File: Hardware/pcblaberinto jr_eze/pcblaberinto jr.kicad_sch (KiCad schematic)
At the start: 19 parts, among them J1 Ultrasonido, J2 Ultrasonido, J3 Ultrasonido, J4 CableAlimentacion, J5 Jumper, J7 EncoderMotorDerecha, J8 EncoderMotorIzquierda, J9 Input of Driver L9110, SW1 SW_Push, U1 L7805

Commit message: modificaciones a la placa
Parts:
- J1, J2, J3: footprint (none) -> EESTN5:pin_strip_4
- UM1: footprint (none) -> EESTN5:ESP32_DEVKITC
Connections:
- net ECCHO_1: now also UM1.9 (IO27); no longer UM1.8 (IO14)
- net IN3: now also J9.5 (Pin_5); no longer J9.6 (Pin_6)
- net IN4: now also J9.6 (Pin_6); no longer J9.5 (Pin_5)
- net TRIGG_1: now also UM1.10 (IO26); no longer UM1.9 (IO27)
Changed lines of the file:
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@@
+    (stroke (width 0) (type default) (color 0 0 0 0))
+  )
+  (wire (pts (xy 120.65 55.88) (xy 124.46 55.88))
     (stroke (width 0) (type default) (color 0 0 0 0))
   )
@@
     (stroke (width 0) (type default) (color 0 0 0 0))
   )
+  (wire (pts (xy 84.9122 111.379) (xy 87.4522 111.379))
+    (stroke (width 0) (type default) (color 0 0 0 0))
+  )
+  (wire (pts (xy 179.705 43.815) (xy 179.705 47.9298))
+    (stroke (width 0) (type default) (color 0 0 0 0))
+  )
+  (wire (pts (xy 256.4638 49.7332) (xy 259.1816 49.7332))
+    (stroke (width 0) (type default) (color 0 0 0 0))
+  )
+  (wire (pts (xy 29.718 50.038) (xy 33.528 50.038))
+    (stroke (width 0) (type default) (color 0 0 0 0))
+  )
+  (wire (pts (xy 188.595 33.655) (xy 191.77 33.655))
+    (stroke (width 0) (type default) (color 0 0 0 0))
+  )
+  (wire (pts (xy 75.057 68.58) (xy 75.057 69.723))
+    (stroke (width 0) (type default) (color 0 0 0 0))
+  )
+  (wire (pts (xy 216.154 29.3624) (xy 216.154 33.655))
+    (stroke (width 0) (type default) (color 0 0 0 0))
+  )
+  (wire (pts (xy 188.595 43.815) (xy 188.595 47.9298))
+    (stroke (width 0) (type default) (color 0 0 0 0))
+  )
+  (wire (pts (xy 248.539 84.455) (xy 254.5588 84.455))
+    (stroke (width 0) (type default) (color 0 0 0 0))
+  )
+  (polyline (pts (xy 62.23 13.335) (xy 62.23 132.08))
+    (stroke (width 0) (type default) (color 0 0 0 0))
+  )
+  (wire (pts (xy 188.595 47.9298) (xy 188.595 47.9552))
+    (stroke (width 0) (type default) (color 0 0 0 0))
+  )
+  (wire (pts (xy 248.539 97.155) (xy 254.5588 97.155))
+    (stroke (width 0) (type default) (color 0 0 0 0))
+  )
+  (wire (pts (xy 29.718 47.498) (xy 33.528 47.498))
+    (stroke (width 0) (type default) (color 0 0 0 0))
+  )
+  (wire (pts (xy 29.972 62.484) (xy 33.782 62.484))
+    (stroke (width 0) (type default) (color 0 0 0 0))
+  )
+  (wire (pts (xy 179.705 38.735) (xy 179.705 33.655))
+    (stroke (width 0) (type default) (color 0 0 0 0))
+  )
+  (polyline (pts (xy 232.41 12.7) (xy 232.41 111.76))
+    (stroke (width 0) (type default) (color 0 0 0 0))
+  )
+  (wire (pts (xy 249.0216 38.9382) (xy 249.0216 42.1132))
+    (stroke (width 0) (type default) (color 0 0 0 0))
+  )
+  (wire (pts (xy 84.9122 113.919) (xy 87.4522 113.919))
+    (stroke (width 0) (type default) (color 0 0 0 0))
+  )
+  (wire (pts (xy 179.705 32.385) (xy 179.705 33.655))
+    (stroke (width 0) (type default) (color 0 0 0 0))
+  )
+  (wire (pts (xy 120.396 45.72) (xy 124.46 45.72))
+    (stroke (width 0) (type default) (color 0 0 0 0))
+  )
+  (wire (pts (xy 216.154 47.9552) (xy 225.425 47.9552))
+    (stroke (width 0) (type default) (color 0 0 0 0))
+  )
+  (wire (pts (xy 29.718 44.958) (xy 33.528 44.958))
+    (stroke (width 0) (type default) (color 0 0 0 0))
+  )
+  (wire (pts (xy 199.39 41.275) (xy 199.39 47.9552))
+    (stroke (width 0) (type default) (color 0 0 0 0))
+  )
+  (wire (pts (xy 87.4522 113.919) (xy 87.4522 114.554))
+    (stroke (width 0) (type default) (color 0 0 0 0))
+  )
+  (wire (pts (xy 119.38 76.2) (xy 119.38 82.55))
+    (stroke (width 0) (type default) (color 0 0 0 0))
+  )
+  (wire (pts (xy 29.718 42.418) (xy 33.528 42.418))
+    (stroke (width 0) (type default) (color 0 0 0 0))
+  )
+  (wire (pts (xy 179.705 47.9298) (xy 188.595 47.9298))
+    (stroke (width 0) (type default) (color 0 0 0 0))
+  )
   (wire (pts (xy 120.65 58.42) (xy 124.46 58.42))
-    (stroke (width 0) (type default) (color 0 0 0 0))
-  )
-  (wire (pts (xy 84.9122 111.379) (xy 87.4522 111.379))
-    (stroke (width 0) (type default) (color 0 0 0 0))
-  )
-  (wire (pts (xy 179.705 43.815) (xy 179.705 47.9298))
-    (stroke (width 0) (type default) (color 0 0 0 0))
-  )
-  (wire (pts (xy 256.4638 49.7332) (xy 259.1816 49.7332))
-    (stroke (width 0) (type default) (color 0 0 0 0))
-  )
-  (wire (pts (xy 29.718 50.038) (xy 33.528 50.038))
-    (stroke (width 0) (type default) (color 0 0 0 0))
-  )
-  (wire (pts (xy 188.595 33.655) (xy 191.77 33.655))
-    (stroke (width 0) (type default) (color 0 0 0 0))
-  )
-  (wire (pts (xy 75.057 68.58) (xy 75.057 69.723))
-    (stroke (width 0) (type default) (color 0 0 0 0))
-  )
-  (wire (pts (xy 216.154 29.3624) (xy 216.154 33.655))
-    (stroke (width 0) (type default) (color 0 0 0 0))
-  )
-  (wire (pts (xy 188.595 43.815) (xy 188.595 47.9298))
-    (stroke (width 0) (type default) (color 0 0 0 0))
-  )
-  (wire (pts (xy 248.539 84.455) (xy 254.5588 84.455))
-    (stroke (width 0) (type default) (color 0 0 0 0))
-  )
-  (polyline (pts (xy 62.23 13.335) (xy 62.23 132.08))
-    (stroke (width 0) (type default) (color 0 0 0 0))
-  )
-  (wire (pts (xy 188.595 47.9298) (xy 188.595 47.9552))
-    (stroke (width 0) (type default) (color 0 0 0 0))
-  )
-  (wire (pts (xy 248.539 97.155) (xy 254.5588 97.155))
-    (stroke (width 0) (type default) (color 0 0 0 0))
-  )
-  (wire (pts (xy 29.718 47.498) (xy 33.528 47.498))
-    (stroke (width 0) (type default) (color 0 0 0 0))
-  )
-  (wire (pts (xy 29.972 62.484) (xy 33.782 62.484))
-    (stroke (width 0) (type default) (color 0 0 0 0))
-  )
-  (wire (pts (xy 179.705 38.735) (xy 179.705 33.655))
-    (stroke (width 0) (type default) (color 0 0 0 0))
-  )
-  (polyline (pts (xy 232.41 12.7) (xy 232.41 111.76))
-    (stroke (width 0) (type default) (color 0 0 0 0))
-  )
-  (wire (pts (xy 249.0216 38.9382) (xy 249.0216 42.1132))
-    (stroke (width 0) (type default) (color 0 0 0 0))
-  )
-  (wire (pts (xy 84.9122 113.919) (xy 87.4522 113.919))
-    (stroke (width 0) (type default) (color 0 0 0 0))
-  )
-  (wire (pts (xy 179.705 32.385) (xy 179.705 33.655))
-    (stroke (width 0) (type default) (color 0 0 0 0))
-  )
-  (wire (pts (xy 120.396 45.72) (xy 124.46 45.72))
-    (stroke (width 0) (type default) (color 0 0 0 0))
-  )
-  (wire (pts (xy 216.154 47.9552) (xy 225.425 47.9552))
-    (stroke (width 0) (type default) (color 0 0 0 0))
-  )
-  (wire (pts (xy 29.718 44.958) (xy 33.528 44.958))
-    (stroke (width 0) (type default) (color 0 0 0 0))
-  )
-  (wire (pts (xy 199.39 41.275) (xy 199.39 47.9552))
-    (stroke (width 0) (type default) (color 0 0 0 0))
-  )
-  (wire (pts (xy 87.4522 113.919) (xy 87.4522 114.554))
-    (stroke (width 0) (type default) (color 0 0 0 0))
-  )
-  (wire (pts (xy 119.38 76.2) (xy 119.38 82.55))
-    (stroke (width 0) (type default) (color 0 0 0 0))
-  )
-  (wire (pts (xy 29.718 42.418) (xy 33.528 42.418))
-    (stroke (width 0) (type default) (color 0 0 0 0))
-  )
-  (wire (pts (xy 120.65 60.96) (xy 124.46 60.96))
-    (stroke (width 0) (type default) (color 0 0 0 0))
-  )
-  (wire (pts (xy 179.705 47.9298) (xy 188.595 47.9298))
     (stroke (width 0) (type default) (color 0 0 0 0))
   )
@@
     (effects (font (size 2 2) (thickness 0.254) bold italic) (justify left bottom))
   )
+  (label "TRIGG_1" (at 120.65 55.88 180)
+    (effects (font (size 1.27 1.27)) (justify right bottom))
+  )
   (label "ECCHO_3" (at 120.396 45.72 180)
     (effects (font (size 1.27 1.27)) (justify right bottom))
@@
     (effects (font (size 1.27 1.27)) (justify right bottom))
   )
+  (label "ECCHO_1" (at 120.65 58.42 180)
+    (effects (font (size 1.27 1.27)) (justify right bottom))
+  )
   (label "IN3" (at 154.94 55.88 0)
     (effects (font (size 1.27 1.27)) (justify left bottom))
-  )
-  (label "TRIGG_1" (at 120.65 58.42 180)
-    (effects (font (size 1.27 1.27)) (justify right bottom))
   )
   (label "VBAT" (at 86.614 88.138 0)
     (effects (font (size 1.524 1.524)) (justify left bottom))
   )
-  (label "ECCHO_1" (at 120.65 60.96 180)
-    (effects (font (size 1.27 1.27)) (justify right bottom))
-  )
   (label "IN4" (at 154.94 58.42 0)
     (effects (font (size 1.27 1.27)) (justify left bottom))
@@
     (effects (font (size 1.27 1.27)) (justify left bottom))
   )
-  (label "IN3" (at 256.4638 49.7332 180)
+  (label "IN4" (at 256.4638 49.7332 180)
     (effects (font (size 1.27 1.27)) (justify right bottom))
   )
@@
     (effects (font (size 1.27 1.27)) (justify right bottom))
   )
-  (label "IN4" (at 256.4892 47.1932 180)
+  (label "IN3" (at 256.4892 47.1932 180)
     (effects (font (size 1.27 1.27)) (justify right bottom))
   )
@@
       (effects (font (size 1.27 1.27)) (justify left))
     )
-    (property "Footprint" "" (id 2) (at 38.608 27.432 0)
+    (property "Footprint" "EESTN5:pin_strip_4" (id 2) (at 38.608 27.432 0)
       (effects (font (size 1.27 1.27)) hide)
     )
@@
       (effects (font (size 1.27 1.27)) (justify left))
     )
-    (property "Footprint" "" (id 2) (at 38.608 44.958 0)
+    (property "Footprint" "EESTN5:pin_strip_4" (id 2) (at 38.608 44.958 0)
       (effects (font (size 1.27 1.27)) hide)
     )
@@
     (property "Reference" "UM1" (id 0) (at 138.43 26.9072 0))
     (property "Value" "ESP32_DEVKITC" (id 1) (at 138.43 29.4441 0))
-    (property "Footprint" "" (id 2) (at 130.81 83.82 0)
+    (property "Footprint" "EESTN5:ESP32_DEVKITC" (id 2) (at 130.81 83.82 0)
       (effects (font (size 1.27 1.27)) hide)
     )
@@
       (effects (font (size 1.27 1.27)) (justify left))
     )
-    (property "Footprint" "" (id 2) (at 38.862 62.484 0)
-      (effects (font (size 1.27 1.27)) hide)
-    )
+    (property "Footprint" "EESTN5:pin_strip_4" (id 2) (at 38.862 62.484 0)
+      (effects (font (size 1.27 1.27)) hide)
+    )

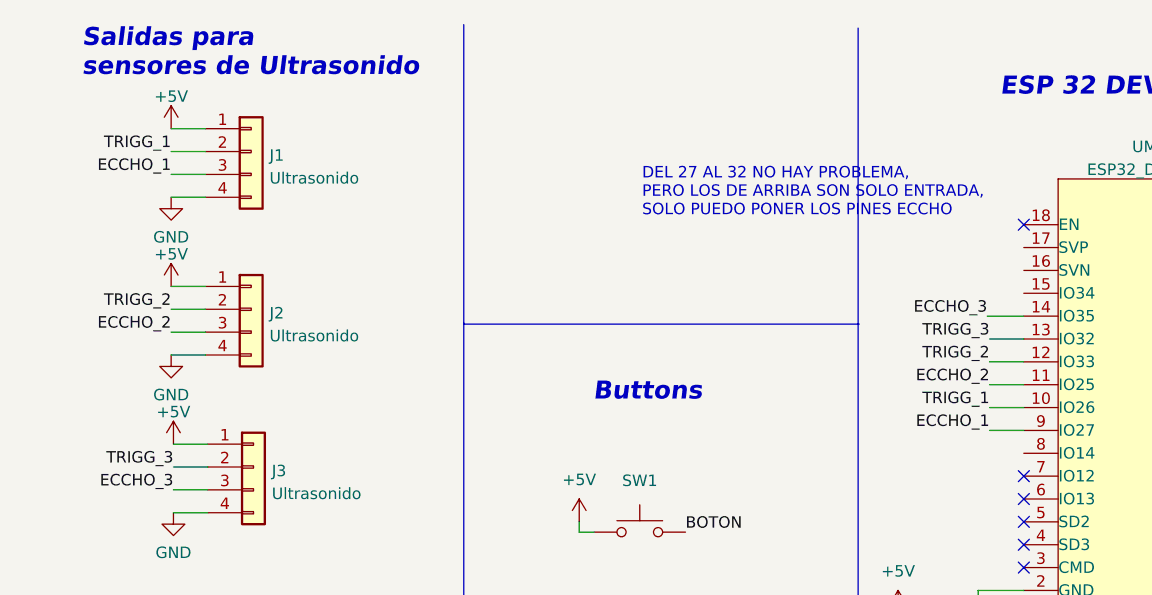
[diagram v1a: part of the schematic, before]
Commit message: cambios en la placa para que los corrija tashe
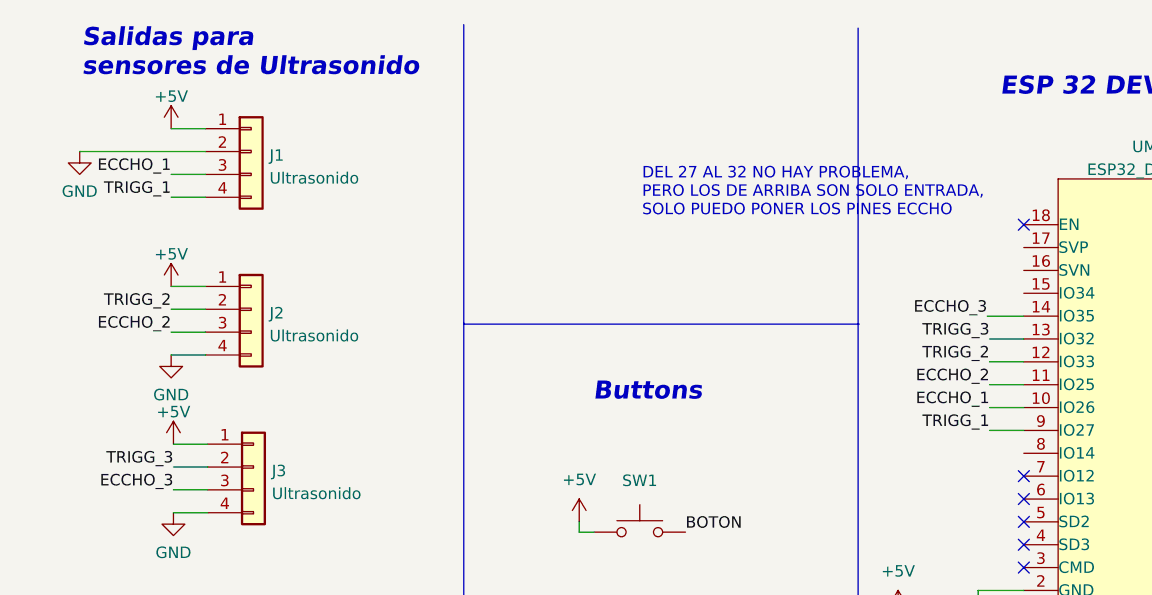
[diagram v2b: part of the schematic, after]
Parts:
- C1, C3: footprint EESTN5:C_1206 -> (none)
- LED1: footprint LED_SMD:LED_1206_3216Metric -> (none)
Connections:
- net ECCHO_1: now also UM1.10 (IO26); no longer UM1.9 (IO27)
- net GND: now also J1.2 (Pin_2); no longer J1.4 (Pin_4)
- net TRIGG_1: now also J1.4 (Pin_4), UM1.9 (IO27); no longer J1.2 (Pin_2), UM1.10 (IO26)
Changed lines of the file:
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@@
+    (stroke (width 0) (type default) (color 0 0 0 0))
+  )
+  (wire (pts (xy 120.65 55.88) (xy 124.46 55.88))
     (stroke (width 0) (type default) (color 0 0 0 0))
   )
@@
     (stroke (width 0) (type default) (color 0 0 0 0))
   )
-  (wire (pts (xy 120.65 55.88) (xy 124.46 55.88))
+  (wire (pts (xy 120.65 58.42) (xy 124.46 58.42))
+    (stroke (width 0) (type default) (color 0 0 0 0))
+  )
+  (wire (pts (xy 33.528 27.432) (xy 19.558 27.432))
     (stroke (width 0) (type default) (color 0 0 0 0))
   )
@@
     (stroke (width 0) (type default) (color 0 0 0 0))
   )
+  (wire (pts (xy 188.595 33.655) (xy 188.595 38.735))
+    (stroke (width 0) (type default) (color 0 0 0 0))
+  )
+  (wire (pts (xy 188.595 47.9552) (xy 199.39 47.9552))
+    (stroke (width 0) (type default) (color 0 0 0 0))
+  )
+  (wire (pts (xy 248.9962 44.6532) (xy 248.9962 45.9994))
+    (stroke (width 0) (type default) (color 0 0 0 0))
+  )
   (wire (pts (xy 29.718 32.512) (xy 33.528 32.512))
     (stroke (width 0) (type default) (color 0 0 0 0))
   )
-  (wire (pts (xy 188.595 33.655) (xy 188.595 38.735))
-    (stroke (width 0) (type default) (color 0 0 0 0))
-  )
-  (wire (pts (xy 188.595 47.9552) (xy 199.39 47.9552))
-    (stroke (width 0) (type default) (color 0 0 0 0))
-  )
-  (wire (pts (xy 248.9962 44.6532) (xy 248.9962 45.9994))
-    (stroke (width 0) (type default) (color 0 0 0 0))
-  )
-  (wire (pts (xy 29.718 27.432) (xy 33.528 27.432))
-    (stroke (width 0) (type default) (color 0 0 0 0))
-  )
   (wire (pts (xy 119.38 76.2) (xy 124.46 76.2))
     (stroke (width 0) (type default) (color 0 0 0 0))
@@
   )
   (wire (pts (xy 179.705 47.9298) (xy 188.595 47.9298))
-    (stroke (width 0) (type default) (color 0 0 0 0))
-  )
-  (wire (pts (xy 120.65 58.42) (xy 124.46 58.42))
     (stroke (width 0) (type default) (color 0 0 0 0))
   )
@@
     (effects (font (size 2 2) (thickness 0.254) bold italic) (justify left bottom))
   )
-  (label "TRIGG_1" (at 120.65 55.88 180)
+  (label "TRIGG_1" (at 29.718 32.512 180)
+    (effects (font (size 1.27 1.27)) (justify right bottom))
+  )
+  (label "TRIGG_1" (at 120.65 58.42 180)
     (effects (font (size 1.27 1.27)) (justify right bottom))
   )
@@
     (effects (font (size 1.27 1.27)) (justify right bottom))
   )
-  (label "ECCHO_1" (at 120.65 58.42 180)
-    (effects (font (size 1.27 1.27)) (justify right bottom))
-  )
   (label "IN3" (at 154.94 55.88 0)
     (effects (font (size 1.27 1.27)) (justify left bottom))
   )
+  (label "ECCHO_1" (at 120.65 55.88 180)
+    (effects (font (size 1.27 1.27)) (justify right bottom))
+  )
   (label "VBAT" (at 86.614 88.138 0)
     (effects (font (size 1.524 1.524)) (justify left bottom))
@@
     (effects (font (size 1.27 1.27)) (justify left bottom))
   )
-  (label "TRIGG_1" (at 29.718 27.432 180)
-    (effects (font (size 1.27 1.27)) (justify right bottom))
-  )
   (label "D0" (at 251.46 86.995 0)
     (effects (font (size 1.27 1.27)) (justify left bottom))
@@
     (pin "1")
   )
-  (symbol (lib_id "power:GND") (at 29.718 32.512 0) (unit 1)
-    (in_bom yes) (on_board yes) (fields_autoplaced)
-    (property "Reference" "#PWR0120" (id 0) (at 29.718 38.862 0)
-      (effects (font (size 1.27 1.27)) hide)
-    )
-    (property "Value" "GND" (id 1) (at 29.718 36.9554 0))
-    (property "Footprint" "" (id 2) (at 29.718 32.512 0)
-      (effects (font (size 1.27 1.27)) hide)
-    )
-    (property "Datasheet" "" (id 3) (at 29.718 32.512 0)
+  (symbol (lib_id "power:GND") (at 19.558 27.432 0) (unit 1)
+    (in_bom yes) (on_board yes) (fields_autoplaced)
+    (property "Reference" "#PWR0120" (id 0) (at 19.558 33.782 0)
+      (effects (font (size 1.27 1.27)) hide)
+    )
+    (property "Value" "GND" (id 1) (at 19.558 31.8754 0))
+    (property "Footprint" "" (id 2) (at 19.558 27.432 0)
+      (effects (font (size 1.27 1.27)) hide)
+    )
+    (property "Datasheet" "" (id 3) (at 19.558 27.432 0)
       (effects (font (size 1.27 1.27)) hide)
     )
@@
       (effects (font (size 1.27 1.27)) (justify left))
     )
-    (property "Footprint" "EESTN5:C_1206" (id 2) (at 210.3374 40.2082 0)
+    (property "Footprint" "" (id 2) (at 210.3374 40.2082 0)
       (effects (font (size 1.27 1.27)) hide)
     )
@@
       (effects (font (size 1.27 1.27)) (justify left))
     )
-    (property "Footprint" "EESTN5:C_1206" (id 2) (at 179.705 41.275 0)
+    (property "Footprint" "" (id 2) (at 179.705 41.275 0)
       (effects (font (size 1.27 1.27)) hide)
     )
@@
       (effects (font (size 1.016 1.016)) (justify left))
     )
-    (property "Footprint" "LED_SMD:LED_1206_3216Metric" (id 2) (at 225.425 39.878 0)
+    (property "Footprint" "" (id 2) (at 225.425 39.878 0)
       (effects (font (size 1.524 1.524)) hide)
     )
@@
     )
     (path "/86966075-cfb9-4128-b802-f9135717e248"
-      (reference "C1") (unit 1) (value "220uF") (footprint "EESTN5:C_1206")
+      (reference "C1") (unit 1) (value "220uF") (footprint "EESTN5:CAP_ELEC_5x11mm")
     )
     (path "/3d045bbb-1fc6-4629-a421-500a2d0c5e89"
@@
     )
     (path "/81518c8d-5fa7-4934-b04c-b4f102784d9b"
-      (reference "C3") (unit 1) (value "220uF") (footprint "EESTN5:C_1206")
+      (reference "C3") (unit 1) (value "220uF") (footprint "EESTN5:CAP_ELEC_5x11mm")
     )
     (path "/f4cdf54e-cfd2-4abf-8201-4bd1f131aee6"
@@
     )
     (path "/d134c16f-ab45-4267-9741-c837e1fb34f0"
-      (reference "LED1") (unit 1) (value "2V") (footprint "LED_SMD:LED_1206_3216Metric")
+      (reference "LED1") (unit 1) (value "2V") (footprint "EESTN5:led_3mm_red")
     )
     (path "/ae8f84b9-8738-4a79-be99-17b739459dee"
